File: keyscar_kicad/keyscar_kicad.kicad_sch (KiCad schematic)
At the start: 29 parts, among them J1 USB_A, P1 USB_C_Plug_USB2.0, SW1 SW_SPDT, SW2 SW_SPDT, SW5_MASTER_EXEC1 SW_Push, SW6_SLAVE_EXEC2 SW_Push

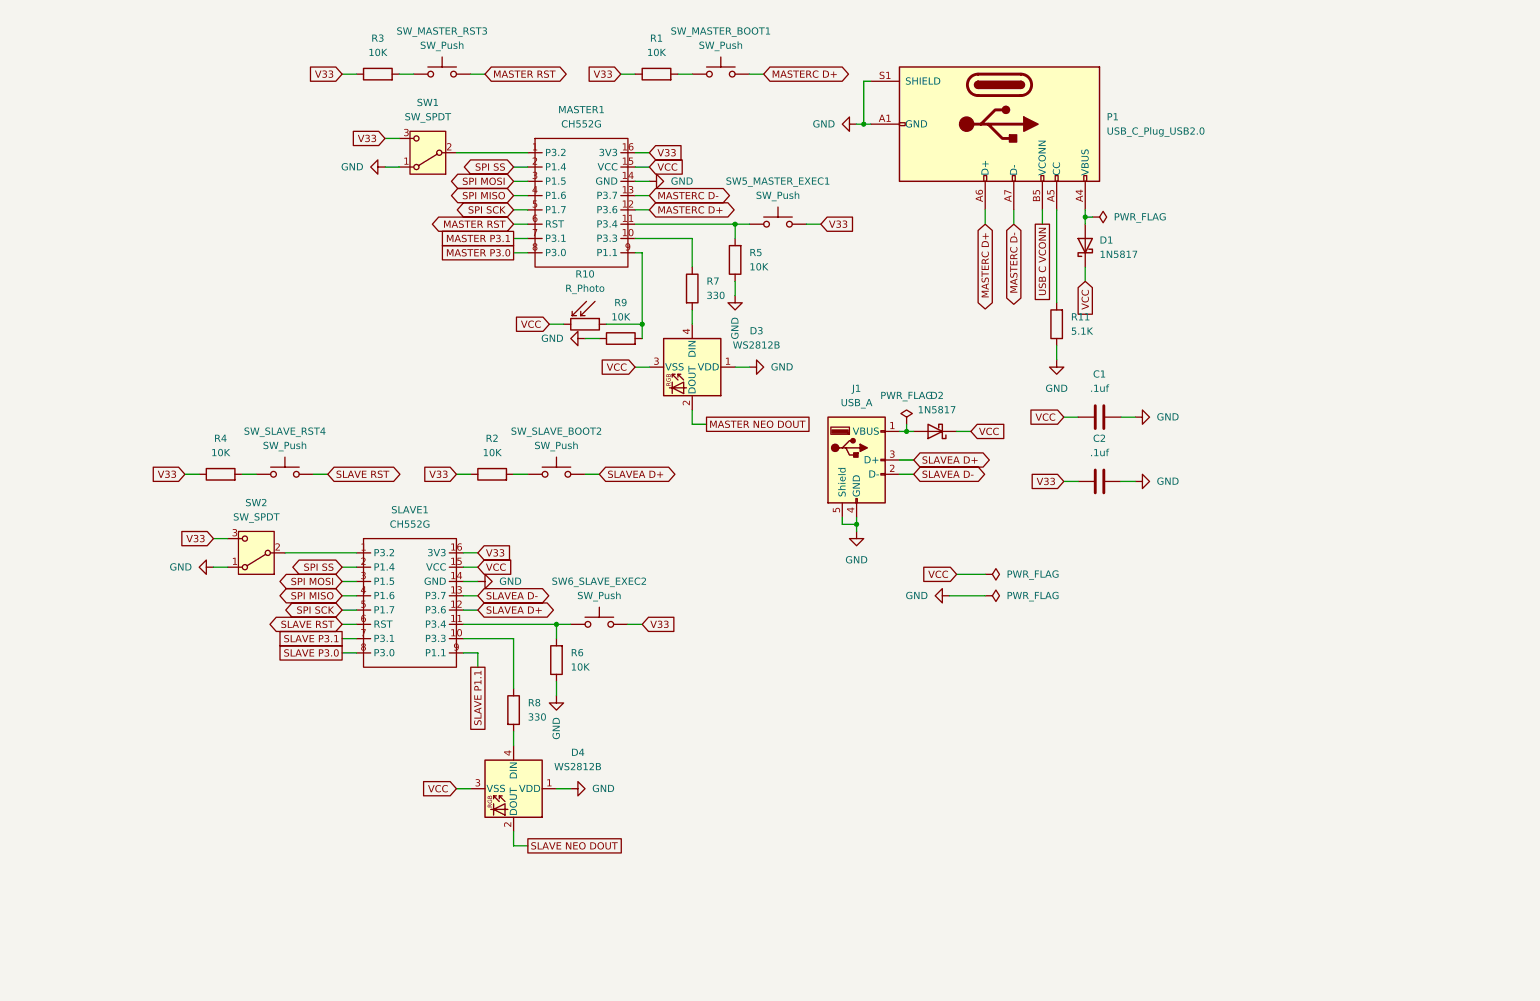
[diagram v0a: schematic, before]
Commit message: Fixing Schematic, Redoing it with Part-Symbols & Connecting footprints, symbols, 3d models alltogether
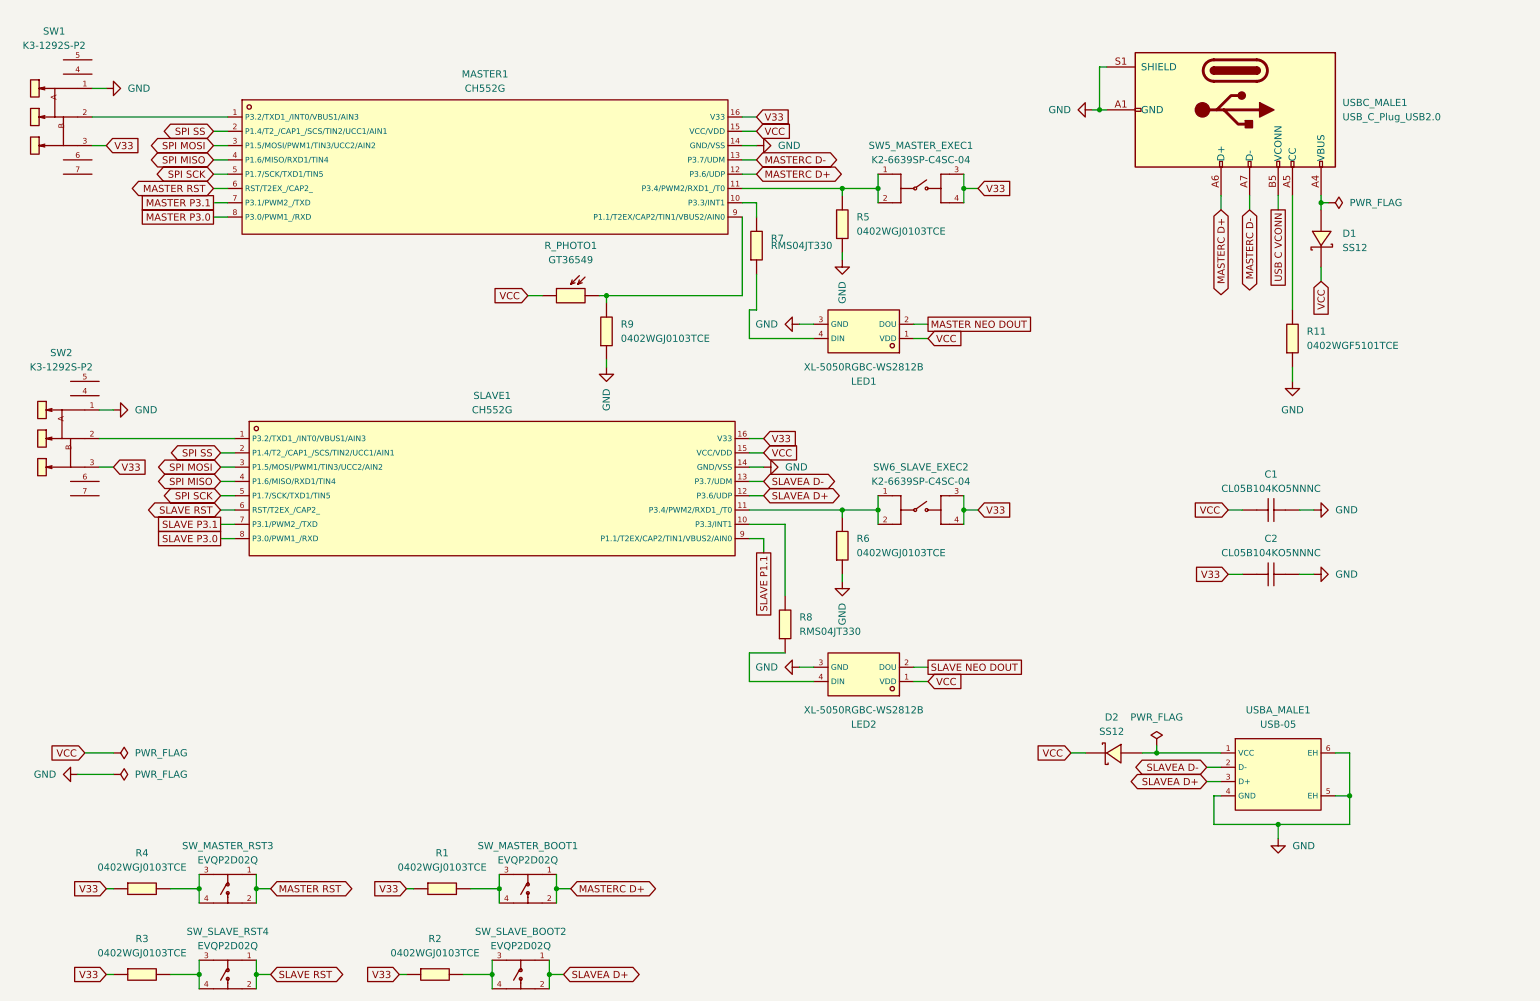
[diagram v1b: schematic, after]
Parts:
- removed C1, C2: .1uf, symbol Device:C
- removed D1, D2: 1N5817, Diode_THT:D_DO-41_SOD81_P10.16mm_Horizontal, symbol Diode:1N5817
- removed D3, D4: WS2812B, LED_SMD:LED_WS2812B_PLCC4_5.0x5.0mm_P3.2mm, symbol LED:WS2812B
- removed J1: USB_A, symbol Connector:USB_A
- removed R1, R2, R3, R4, R5, R6, R9: 10K, symbol Device:R
- removed R10: R_Photo, symbol Device:R_Photo
- removed R11: 5.1K, symbol Device:R
- removed R7, R8: 330, symbol Device:R
- removed SW1, SW2: SW_SPDT, symbol Switch:SW_SPDT
- removed SW5_MASTER_EXEC1, SW6_SLAVE_EXEC2, SW_MASTER_BOOT1, SW_MASTER_RST3, SW_SLAVE_BOOT2, SW_SLAVE_RST4: SW_Push, symbol Switch:SW_Push
- added C1, C2: CL05B104KO5NNNC, Library:C0402, symbol CL05B104KO5NNNC:CL05B104KO5NNNC
- added D1, D2: SS12, Library:SMA_L4.3-W2.6-LS5.2-RD, symbol SS12:SS12
- added LED1, LED2: XL-5050RGBC-WS2812B, Library:LED-SMD_4P-L5.0-W5.0-BL_XL-5050RGBC, symbol XL-5050RGBC-WS2812B:XL-5050RGBC-WS2812B
- added R1, R2, R3, R4, R5, R6, R9: 0402WGJ0103TCE, Library:R0402, symbol 0402WGJ0103TCE:0402WGJ0103TCE
- added R11: 0402WGF5101TCE, Library:R0402, symbol 0402WGF5101TCE:0402WGF5101TCE
- added R7, R8: RMS04JT330, Library:R0402, symbol RMS04JT330:RMS04JT330
- added R_PHOTO1: GT36549, Library:RES-SMD_L3.6-W2.4, symbol GT36549:GT36549
- added SW1, SW2: K3-1292S-P2, Library:SW-SMD_K3-1292S-P2, symbol K3-1292S-P2:K3-1292S-P2
- added SW5_MASTER_EXEC1, SW6_SLAVE_EXEC2: K2-6639SP-C4SC-04, Library:KEY-SMD_4P-L6.0-W6.0-P3.90-LS9.0, symbol K2-6639SP-C4SC-04:K2-6639SP-C4SC-04
- added SW_MASTER_BOOT1, SW_MASTER_RST3, SW_SLAVE_BOOT2, SW_SLAVE_RST4: EVQP2D02Q, Library:KEY-SMD_4P-L4.7-W3.5-P1.70-LS5.5, symbol EVQP2D02Q:EVQP2D02Q
- added USBA_MALE1: USB-05, Library:USB-A-TH_USB-05, symbol USB-05:USB-05
- MASTER1, SLAVE1: footprint (none) -> Library:SOP-16_L10.0-W3.9-P1.27-LS6.0-BL; LCSC (none) -> C111292
- USBC_MALE1: renamed from P1; footprint (none) -> Connector_USB:USB_C_Plug_Molex_105444
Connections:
- net GND: now also C1.2, C2.2, LED1.3 (GND), LED2.3 (GND), R11.1, R5.1, R6.1, R9.1, SW1.1, SW2.1, USBA_MALE1.4 (GND), USBA_MALE1.5 (EH), USBA_MALE1.6 (EH)
- net MASTER NEO DOUT: now also LED1.2 (DOU)
- net MASTER RST: now also SW_MASTER_RST3.1, SW_MASTER_RST3.2
- net MASTERC D+: now also SW_MASTER_BOOT1.1, SW_MASTER_BOOT1.2
- net SLAVE NEO DOUT: now also LED2.2 (DOU)
- net SLAVE RST: now also SW_SLAVE_RST4.1, SW_SLAVE_RST4.2
- net SLAVEA D+: now also SW_SLAVE_BOOT2.1, SW_SLAVE_BOOT2.2, USBA_MALE1.3 (D+)
- net SLAVEA D-: now also USBA_MALE1.2 (D-)
- net V33: now also C2.1, R1.1, R2.1, R3.1, R4.1, SW1.3, SW2.3, SW5_MASTER_EXEC1.3, SW5_MASTER_EXEC1.4, SW6_SLAVE_EXEC2.3, SW6_SLAVE_EXEC2.4
- net VCC: now also C1.1, D1.1 (K), D2.1 (K), LED1.1 (VDD), LED2.1 (VDD), R_PHOTO1.1
- net at MASTER1.9 (P1.1/T2EX/CAP2/TIN1/VBUS2/AIN0): now also R9.2, R_PHOTO1.2
- net at USBC_MALE1.A4 (VBUS), USBC_MALE1.A9 (VBUS), USBC_MALE1.B4 (VBUS)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: now also D1.2 (A)
- net at USBC_MALE1.A5 (CC): now also R11.2
- net at SLAVE1.10 (P3.3/INT1): now also R8.2
- net at SLAVE1.1 (P3.2/TXD1_/INT0/VBUS1/AIN3): now also SW2.2
- net at MASTER1.1 (P3.2/TXD1_/INT0/VBUS1/AIN3): now also SW1.2
- net at MASTER1.10 (P3.3/INT1): now also R7.2
- net at MASTER1.11 (P3.4/PWM2/RXD1_/T0): now also R5.2, SW5_MASTER_EXEC1.1, SW5_MASTER_EXEC1.2
- net at SLAVE1.11 (P3.4/PWM2/RXD1_/T0): now also R6.2, SW6_SLAVE_EXEC2.1, SW6_SLAVE_EXEC2.2
- new net: R4.2, SW_MASTER_RST3.3, SW_MASTER_RST3.4
- new net: R1.2, SW_MASTER_BOOT1.3, SW_MASTER_BOOT1.4
- new net: R2.2, SW_SLAVE_BOOT2.3, SW_SLAVE_BOOT2.4
- new net: LED2.4 (DIN), R8.1
- new net: LED1.4 (DIN), R7.1
- new net: D2.2 (A), USBA_MALE1.1 (VCC)
- new net: R3.2, SW_SLAVE_RST4.3, SW_SLAVE_RST4.4
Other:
- moved on the sheet: USBC_MALE1

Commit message: Getting Started on Wiring the PCB & Substituting Parts
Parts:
- removed D1, D2: SS12, Library:SMA_L4.3-W2.6-LS5.2-RD, symbol SS12:SS12
- removed R3: 0402WGJ0103TCE, Library:R0402, symbol 0402WGJ0103TCE:0402WGJ0103TCE
- removed SW5_MASTER_EXEC1, SW6_SLAVE_EXEC2: K2-6639SP-C4SC-04, Library:KEY-SMD_4P-L6.0-W6.0-P3.90-LS9.0, symbol K2-6639SP-C4SC-04:K2-6639SP-C4SC-04
- removed SW_SLAVE_RST4: EVQP2D02Q, Library:KEY-SMD_4P-L4.7-W3.5-P1.70-LS5.5, symbol EVQP2D02Q:EVQP2D02Q
- added D1, D2: B5817W_C8597, Library:SOD-123_L2.8-W1.8-LS3.7-RD, symbol B5817W_C8597:B5817W_C8597
- added SW5_MASTER_EXEC1, SW6_SLAVE_EXEC2: TSA453G50-250, Library:KEY-SMD_4P-L4.5-W4.5-P3.00-LS7.5, symbol TSA453G50-250:TSA453G50-250
- renumbered SW_MASTER_RST3 to SW_CHIP_RST3
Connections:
- net SLAVE RST is gone; now on net MASTER RST: SLAVE1.6 (RST/T2EX_/CAP2_)
- net V33: now also SW5_MASTER_EXEC1.1, SW5_MASTER_EXEC1.3, SW6_SLAVE_EXEC2.1, SW6_SLAVE_EXEC2.3; no longer R4.1
- net VCC: now also R4.1, D1.1 (C), D2.1 (C)
- net at USBC_MALE1.A4 (VBUS), USBC_MALE1.A9 (VBUS), USBC_MALE1.B4 (VBUS)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: now also D1.2 (A)
- net at R6.2, SLAVE1.11 (P3.4/PWM2/RXD1_/T0): now also SW6_SLAVE_EXEC2.2, SW6_SLAVE_EXEC2.4
- net at USBA_MALE1.1 (VCC): now also D2.2 (A)
- net at MASTER1.11 (P3.4/PWM2/RXD1_/T0), R5.2: now also SW5_MASTER_EXEC1.2, SW5_MASTER_EXEC1.4

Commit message: Wrapping up the PCB, wiring the VCC, V33, GND
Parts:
- removed SW1, SW2: K3-1292S-P2, Library:SW-SMD_K3-1292S-P2, symbol K3-1292S-P2:K3-1292S-P2
- removed USBC_MALE1: USB_C_Plug_USB2.0, Connector_USB:USB_C_Plug_Molex_105444, symbol Connector:USB_C_Plug_USB2.0
- added R3: 0402WGF5101TCE, Library:R0402, symbol 0402WGF5101TCE:0402WGF5101TCE
- added SW1, SW2: SSSS211603, Library:SW-SMD_SSSS211603, symbol SSSS211603:SSSS211603
- added USBC_MALE1: 918-118A2021S40003, Library:USB-C-SMD_918-118A2021S40003, symbol 918-118A2021S40003:918-118A2021S40003
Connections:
- net GND: now also R3.1, SW1.1, SW2.1, USBC_MALE1.1 (EP), USBC_MALE1.2 (EP), USBC_MALE1.3 (EP), USBC_MALE1.4 (EP), USBC_MALE1.A1 (GND), USBC_MALE1.A12 (GND), USBC_MALE1.B1 (GND), USBC_MALE1.B12 (GND)
- net MASTERC D+: now also USBC_MALE1.A6 (DP1), USBC_MALE1.B6 (DP2)
- net MASTERC D-: now also USBC_MALE1.A7 (DN1), USBC_MALE1.B7 (DN2)
- net V33: now also SW1.3, SW2.3
- net USB C VBUS: now reaches D1.2 (A)
- net USB C VBUS: now also USBC_MALE1.A4 (VBUS), USBC_MALE1.A9 (VBUS), USBC_MALE1.B4 (VBUS), USBC_MALE1.B9 (VBUS)
- net at R11.2: now also USBC_MALE1.A5 (CC1)
- net at SLAVE1.1 (P3.2/TXD1_/INT0/VBUS1/AIN3): now also SW2.2
- net at MASTER1.1 (P3.2/TXD1_/INT0/VBUS1/AIN3): now also SW1.2
- new net: R3.2, USBC_MALE1.B5 (CC2)
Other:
- moved on the sheet: D1, R11

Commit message: safety commit again
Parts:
- removed SW_CHIP_RST3, SW_MASTER_BOOT1, SW_SLAVE_BOOT2: EVQP2D02Q, Library:KEY-SMD_4P-L4.7-W3.5-P1.70-LS5.5, symbol EVQP2D02Q:EVQP2D02Q
- removed USBC_MALE1: 918-118A2021S40003, Library:USB-C-SMD_918-118A2021S40003, symbol 918-118A2021S40003:918-118A2021S40003
- added SW_CHIP_RST3, SW_MASTER_BOOT1, SW_SLAVE_BOOT2: EVQP2202M, Library:SW-SMD_L4.7-W3.5-P2.00-LS5.2_EVQP2202M, symbol EVQP2202M:EVQP2202M
- added USBC_MALE1: 918-118A2021Y40005, Library:USB-C-SMD_918-118A2021Y40005, symbol 918-118A2021Y40005:918-118A2021Y40005
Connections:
- net GND: now also USBC_MALE1.A1 (GND), USBC_MALE1.A12 (GND), USBC_MALE1.B1 (GND), USBC_MALE1.SH1 (EH), USBC_MALE1.SH2 (EH), USBC_MALE1.SH3 (EH), USBC_MALE1.SH4 (EH)
- net MASTER RST: now also SW_CHIP_RST3.1, SW_CHIP_RST3.2
- net MASTERC D+: now also SW_MASTER_BOOT1.1, SW_MASTER_BOOT1.2, USBC_MALE1.A6 (DP1), USBC_MALE1.B6 (DP2)
- net MASTERC D-: now also USBC_MALE1.A7 (DN1), USBC_MALE1.B7 (DN2)
- net SLAVEA D+: now also SW_SLAVE_BOOT2.1, SW_SLAVE_BOOT2.2
- net USB C VBUS: now also USBC_MALE1.A4 (VBUS), USBC_MALE1.A9 (VBUS), USBC_MALE1.B4 (VBUS), USBC_MALE1.B9 (VBUS)
- net at R4.2: now also SW_CHIP_RST3.3, SW_CHIP_RST3.4
- net at R1.2: now also SW_MASTER_BOOT1.3, SW_MASTER_BOOT1.4
- net at R2.2: now also SW_SLAVE_BOOT2.3, SW_SLAVE_BOOT2.4
- net at R3.2: now also USBC_MALE1.B5 (CC2)
- net at R11.2: now also USBC_MALE1.A5 (CC1)
